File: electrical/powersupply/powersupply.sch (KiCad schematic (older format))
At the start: 18 parts, among them J1 Barrel_Jack_Switch, J2 Conn_01x02_Female, U1 TPS54232

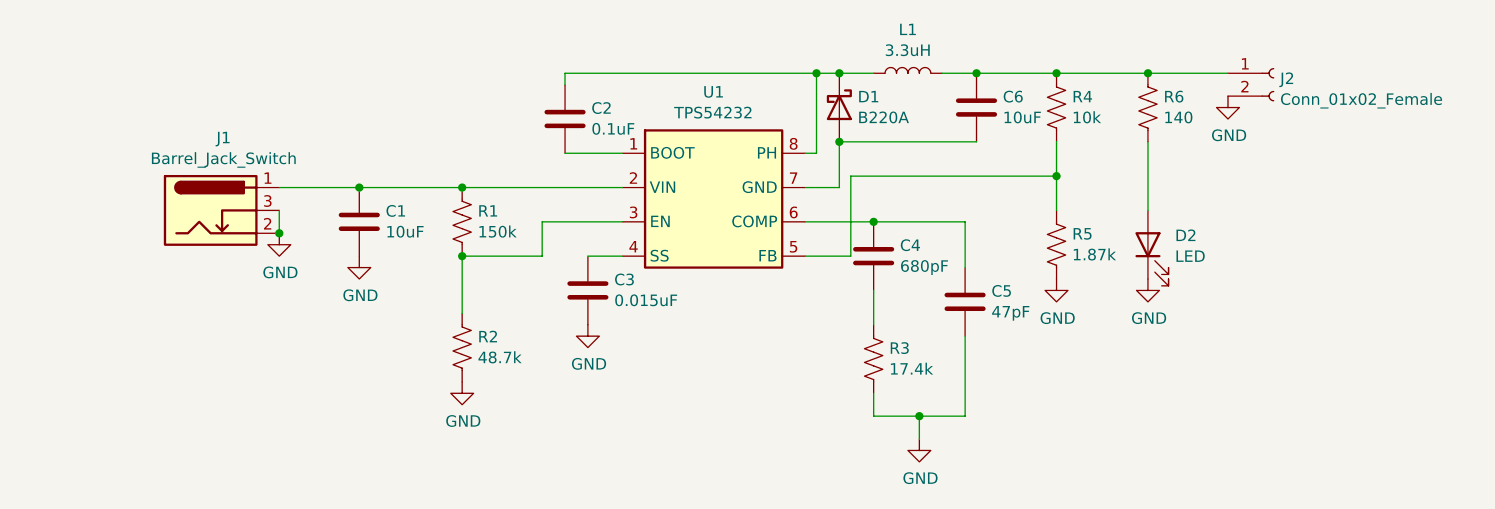
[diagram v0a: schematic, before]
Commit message: Revised power supply design and completed new PCB layout
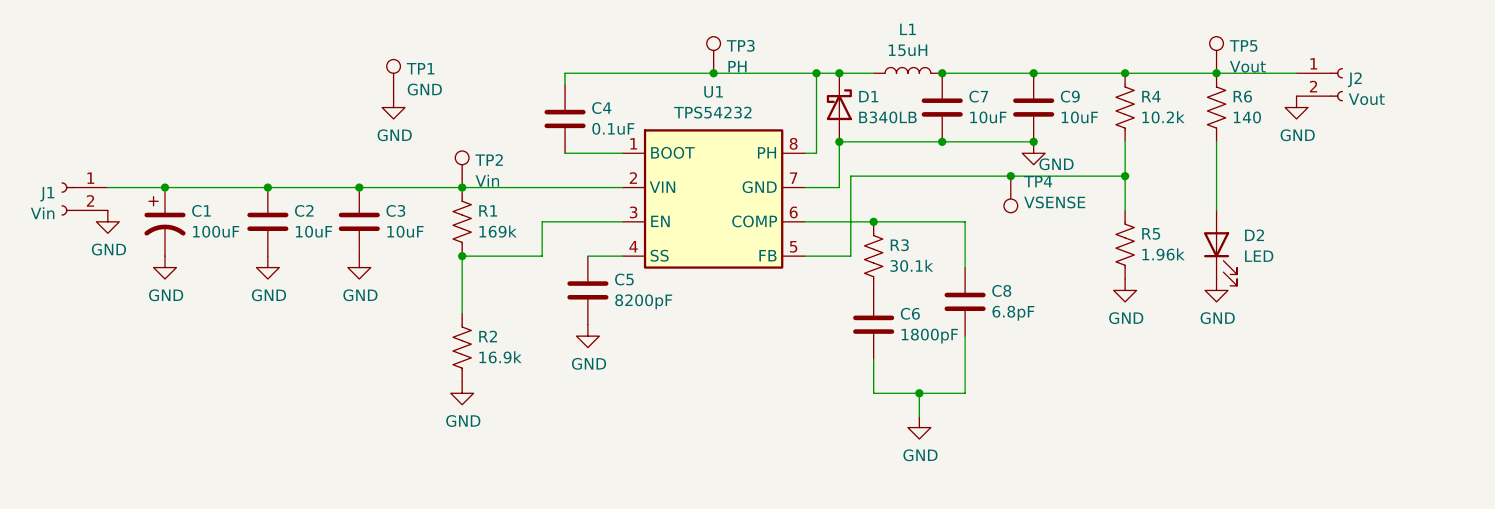
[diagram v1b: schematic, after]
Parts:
- removed D1: B220A, Diode_SMD:D_SMA_Handsoldering, symbol Capstone:B220A
- removed J1: Barrel_Jack_Switch, Connector_BarrelJack:BarrelJack_CUI_PJ-102AH_Horizontal, symbol Connector:Barrel_Jack_Switch
- added C1: 100uF, Capacitor_THT:CP_Radial_D6.3mm_P2.50mm, symbol Device:CP1
- added C3: 10uF, Capacitor_SMD:C_1210_3225Metric_Pad1.33x2.70mm_HandSolder, symbol Device:C
- added C9: 10uF, Capacitor_SMD:C_0805_2012Metric_Pad1.18x1.45mm_HandSolder, symbol Device:C
- added D1: B340LB, Diode_SMD:D_SMB_Handsoldering, symbol Device:D_Schottky
- added J1: Vin, Connector_PinHeader_2.54mm:PinHeader_1x02_P2.54mm_Vertical, symbol Connector:Conn_01x02_Female
- added TP1: GND, TestPoint:TestPoint_Pad_D1.5mm, symbol Connector:TestPoint
- added TP2: Vin, TestPoint:TestPoint_Pad_D1.5mm, symbol Connector:TestPoint
- added TP3: PH, TestPoint:TestPoint_Pad_D1.5mm, symbol Connector:TestPoint
- added TP4: VSENSE, TestPoint:TestPoint_Pad_D1.5mm, symbol Connector:TestPoint
- added TP5: Vout, TestPoint:TestPoint_Pad_D1.5mm, symbol Connector:TestPoint
- C2: renamed from C1; footprint Capacitor_SMD:C_0805_2012Metric_Pad1.18x1.45mm_HandSolder -> Capacitor_SMD:C_1210_3225Metric_Pad1.33x2.70mm_HandSolder; MFN (none) -> CL32B106KBJZW6E
- C4: renamed from C2; MFN (none) -> CL10B104KO8NFNC
- C5: renamed from C3; value 0.015uF -> 8200pF; footprint Capacitor_SMD:C_0603_1608Metric_Pad1.08x0.95mm_HandSolder -> Capacitor_SMD:C_0805_2012Metric_Pad1.18x1.45mm_HandSolder; MFN (none) -> CL21B822KBANNNC
- C6: renamed from C4; value 680pF -> 1800pF; MFN (none) -> CL10C182JB8NNNC
- C7: renamed from C6; MFN (none) -> CL21A106KAYNNNG
- C8: renamed from C5; value 47pF -> 6.8pF; MFN (none) -> CL10C6R8CB8NNNC
- D2: MFN (none) -> ‎SML-D12P8WT86‎
- J2: value Conn_01x02_Female -> Vout
- L1: value 3.3uH -> 15uH; footprint Inductor_SMD:L_Taiyo-Yuden_NR-50xx_HandSoldering -> Inductor_SMD:L_7.3x7.3_H4.5; MFN (none) -> CDRH74NP-150MC-B
- R1: value 150k -> 169k; footprint Resistor_SMD:R_0603_1608Metric_Pad0.98x0.95mm_HandSolder -> Resistor_SMD:R_0805_2012Metric_Pad1.20x1.40mm_HandSolder; MFN (none) -> RMCF0805FT169K
- R2: value 48.7k -> 16.9k; footprint Resistor_SMD:R_0603_1608Metric_Pad0.98x0.95mm_HandSolder -> Resistor_SMD:R_0805_2012Metric_Pad1.20x1.40mm_HandSolder; MFN (none) -> RMCF0805FT16K9
- R3: value 17.4k -> 30.1k; footprint Resistor_SMD:R_0603_1608Metric_Pad0.98x0.95mm_HandSolder -> Resistor_SMD:R_0805_2012Metric_Pad1.20x1.40mm_HandSolder; MFN (none) -> RMCF0805FT30K1
- R4: value 10k -> 10.2k; footprint Resistor_SMD:R_0603_1608Metric_Pad0.98x0.95mm_HandSolder -> Resistor_SMD:R_0805_2012Metric_Pad1.20x1.40mm_HandSolder; MFN (none) -> RMCF0805FT10K2
- R5: value 1.87k -> 1.96k; footprint Resistor_SMD:R_0603_1608Metric_Pad0.98x0.95mm_HandSolder -> Resistor_SMD:R_0805_2012Metric_Pad1.20x1.40mm_HandSolder; MFN (none) -> RMCF0805FT1K96
- R6: footprint Resistor_SMD:R_0603_1608Metric_Pad0.98x0.95mm_HandSolder -> Resistor_SMD:R_0805_2012Metric_Pad1.20x1.40mm_HandSolder; MFN (none) -> RMCF0805FT140R
- U1: MFN (none) -> TPS54232D
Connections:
- net GND: now also C6.2, C7.2, U1.7 (GND), C1.2, C3.2, C9.2, D1.2 (A), J1.2 (Pin_2), TP1.1; no longer R3.2
- net at C2.1, R1.1, U1.2 (VIN): now also C1.1, C3.1, J1.1 (Pin_1), TP2.1
- net at R4.2, R5.1, U1.5 (FB): now also TP4.1
- net at C8.1, U1.6 (COMP): now also R3.1; no longer C6.1
- net at C4.1, L1.1, U1.8 (PH): now also D1.1 (K), TP3.1
- net at C7.1, J2.1 (Pin_1), L1.2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: now also C9.1, TP5.1
- new net: C6.1, R3.2
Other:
- moved on the sheet: C2, C6, C7, D2, J2, R3, R4, R5, R6
